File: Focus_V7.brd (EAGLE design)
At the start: 64.8 x 94 mm, 100 parts, among them X1 USB+SHIELD, Y1 16Mhz

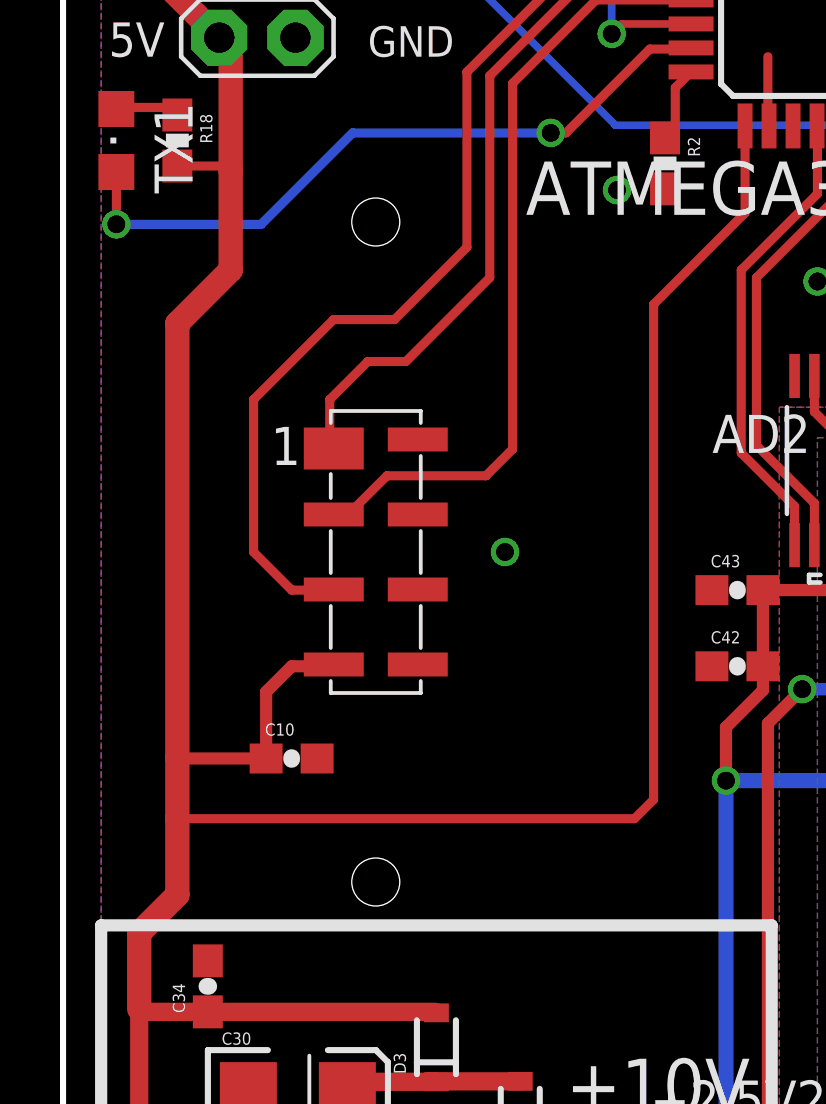
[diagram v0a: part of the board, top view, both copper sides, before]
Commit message: Changed hole size from 1.6 to 2.2mm for TSL1401CL shroud
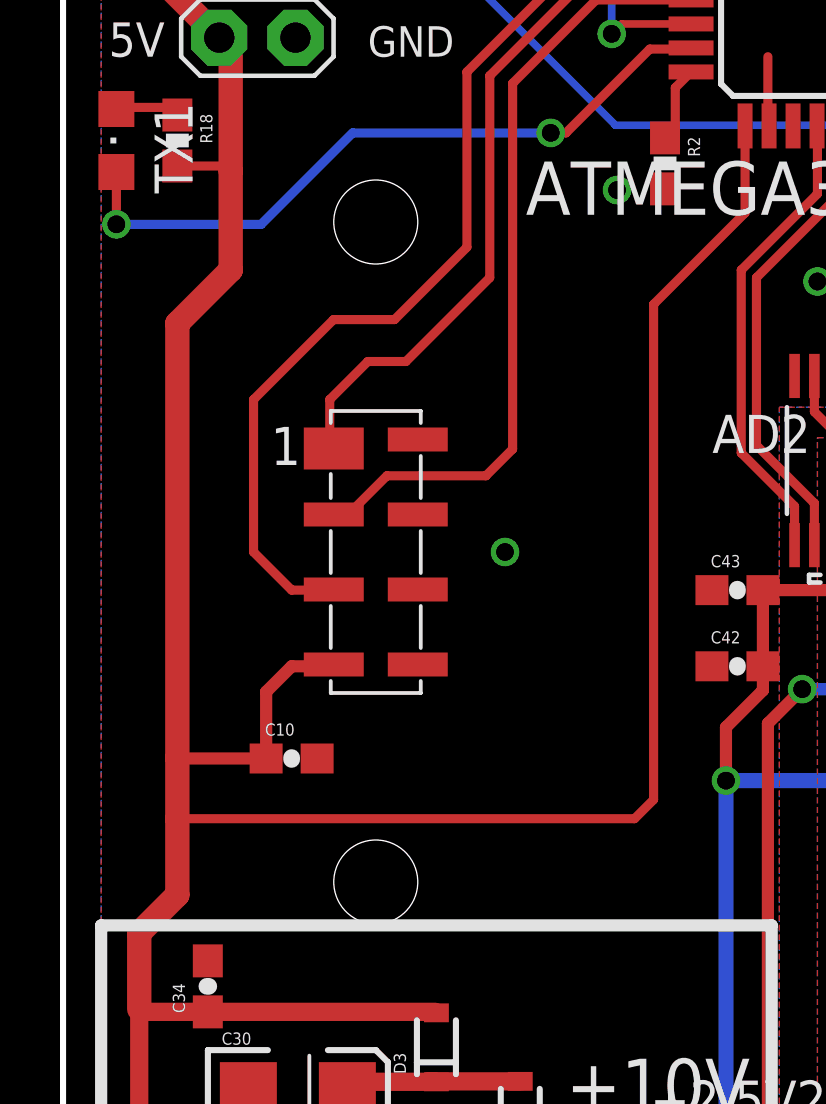
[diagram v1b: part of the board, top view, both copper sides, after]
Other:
- board text added: "Adafruit Industries"
- board text added: "Parallax Inc"
- board text added: "Sparkfun Electronics"
- board text removed: "Adafruit"
- board text removed: "Sparkfun"
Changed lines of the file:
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@@
 <layer number="50" name="dxf" color="7" fill="1" visible="no" active="yes"/>
 <layer number="51" name="tDocu" color="6" fill="1" visible="yes" active="yes"/>
-<layer number="52" name="bDocu" color="7" fill="1" visible="no" active="yes"/>
+<layer number="52" name="bDocu" color="7" fill="1" visible="yes" active="yes"/>
 <layer number="53" name="tGND_GNDA" color="7" fill="9" visible="no" active="no"/>
 <layer number="54" name="bGND_GNDA" color="1" fill="9" visible="no" active="no"/>
@@
 <hole x="96.52" y="2.54" drill="3.2"/>
 <text x="74.93" y="21.59" size="1.778" layer="22" rot="MR0">Arduino Team</text>
-<text x="74.93" y="17.78" size="1.778" layer="22" rot="MR0">Sparkfun</text>
-<text x="74.93" y="13.97" size="1.778" layer="22" rot="MR0">Adafruit</text>
+<text x="74.93" y="17.78" size="1.778" layer="22" rot="MR0">Sparkfun Electronics</text>
+<text x="74.93" y="13.97" size="1.778" layer="22" rot="MR0">Adafruit Industries</text>
 <wire x1="44.45" y1="24.13" x2="82.55" y2="24.13" width="0.254" layer="22"/>
 <wire x1="77.724" y1="32.512" x2="80.264" y2="32.512" width="0.3048" layer="41"/>
@@
 <wire x1="75.184" y1="66.167" x2="75.311" y2="66.294" width="0.3048" layer="42"/>
 <wire x1="76.581" y1="67.691" x2="76.708" y2="67.818" width="0.3048" layer="42"/>
+<text x="74.93" y="10.16" size="1.778" layer="22" rot="MR0">Parallax Inc</text>
 </plain>
 <attributes>
@@
 <via x="70.358" y="36.83" extent="1-16" drill="0.6"/>
 <via x="80.391" y="38.1" extent="1-16" drill="0.6"/>
+<wire x1="64.516" y1="51.5874" x2="63.1952" y2="51.5874" width="0" layer="19" extent="1-1"/>
 </signal>
 <signal name="TSL1401R_A0">

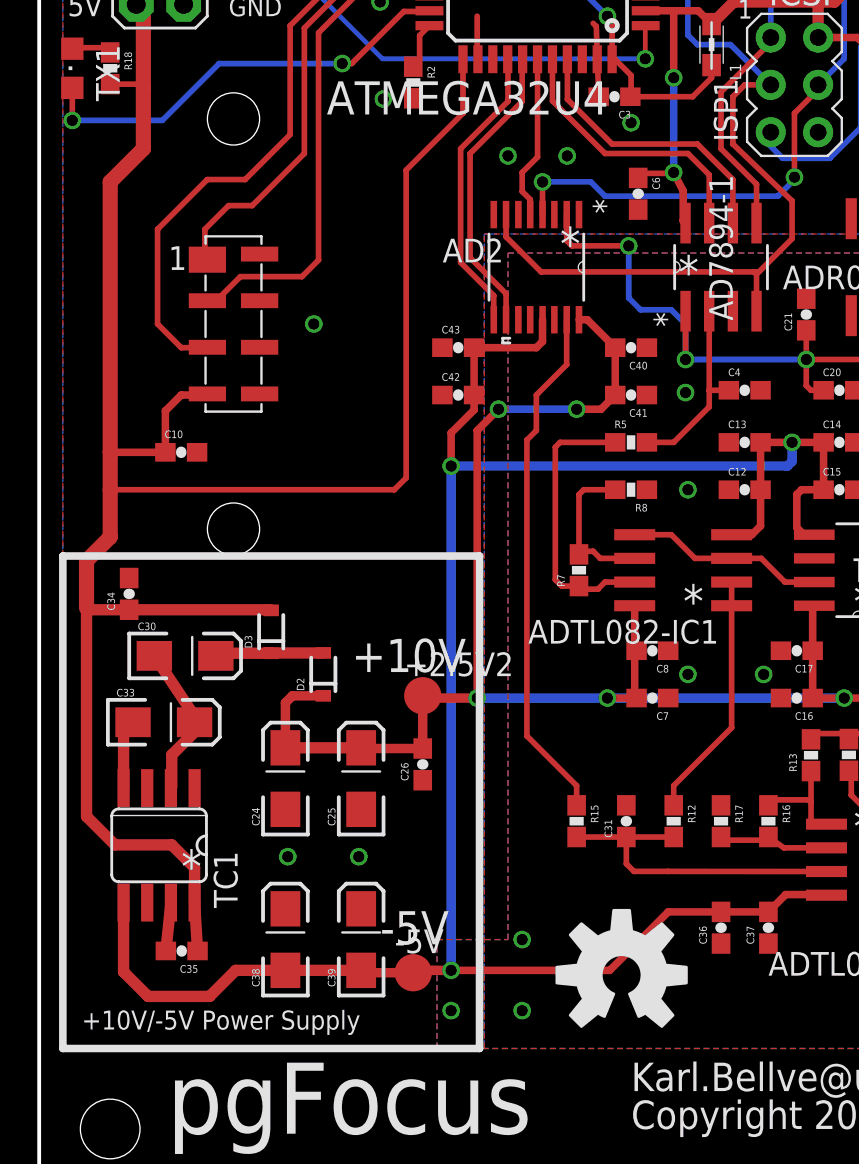
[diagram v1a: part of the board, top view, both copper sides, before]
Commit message: Pin 7 of TC7660 has a capacitor labeled C35, which should have been connected to ground, and not 5V This has been corrected in this revision. C35 is optional, and not needed. Only use if trying to slow down OSC for lower current.
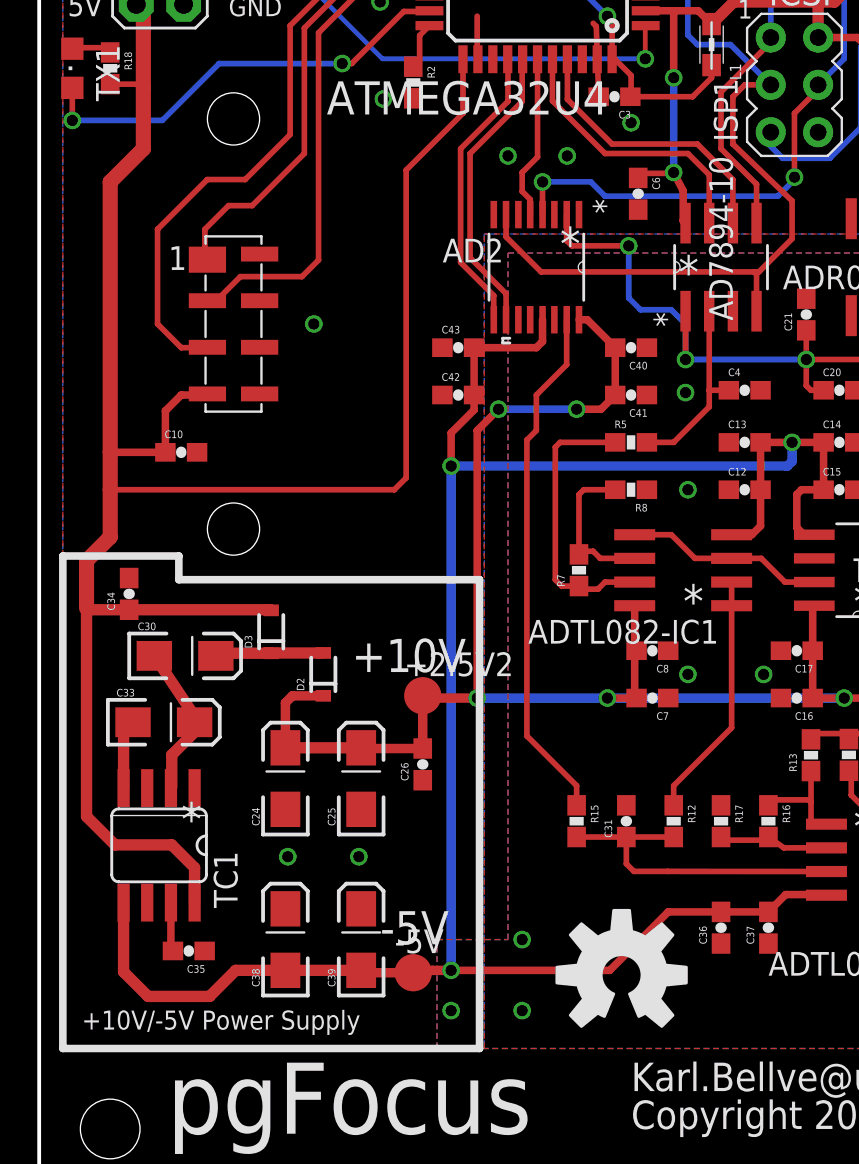
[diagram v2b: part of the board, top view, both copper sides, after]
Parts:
- moved C35 0.38 mm to (43.6, 12.1)
- renumbered AD7894-1 to AD7894-10
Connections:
- net +5V: no longer C35.1
- net GND: now also C35.1
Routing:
- net +5V: track 324.1 -> 321.5 mm
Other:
- board text added: "Optional Cap (C35) to"
- board text added: "slow the OSC (pin 7)"
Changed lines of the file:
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@@
 <layer number="39" name="tKeepout" color="4" fill="11" visible="no" active="yes"/>
 <layer number="40" name="bKeepout" color="1" fill="11" visible="no" active="yes"/>
-<layer number="41" name="tRestrict" color="4" fill="10" visible="no" active="yes"/>
-<layer number="42" name="bRestrict" color="1" fill="10" visible="no" active="yes"/>
+<layer number="41" name="tRestrict" color="4" fill="10" visible="yes" active="yes"/>
+<layer number="42" name="bRestrict" color="1" fill="10" visible="yes" active="yes"/>
 <layer number="43" name="vRestrict" color="2" fill="10" visible="no" active="yes"/>
 <layer number="44" name="Drills" color="7" fill="1" visible="no" active="yes"/>
@@
 <layer number="50" name="dxf" color="7" fill="1" visible="no" active="yes"/>
 <layer number="51" name="tDocu" color="6" fill="1" visible="yes" active="yes"/>
-<layer number="52" name="bDocu" color="7" fill="1" visible="yes" active="yes"/>
+<layer number="52" name="bDocu" color="7" fill="1" visible="no" active="yes"/>
 <layer number="53" name="tGND_GNDA" color="7" fill="9" visible="no" active="no"/>
 <layer number="54" name="bGND_GNDA" color="1" fill="9" visible="no" active="no"/>
@@
 <wire x1="94.488" y1="46.228" x2="95.123" y2="44.831" width="0.3048" layer="42"/>
 <wire x1="95.123" y1="44.831" x2="94.996" y2="43.18" width="0.3048" layer="42"/>
-<wire x1="59.182" y1="33.274" x2="36.83" y2="33.274" width="0.4064" layer="21"/>
-<wire x1="59.182" y1="33.274" x2="59.182" y2="6.858" width="0.4064" layer="21"/>
+<wire x1="59.182" y1="32.004" x2="43.053" y2="32.004" width="0.4064" layer="21"/>
+<wire x1="43.053" y1="32.004" x2="43.053" y2="33.274" width="0.4064" layer="21"/>
+<wire x1="43.053" y1="33.274" x2="36.83" y2="33.274" width="0.4064" layer="21"/>
+<wire x1="59.182" y1="32.004" x2="59.182" y2="6.858" width="0.4064" layer="21"/>
 <wire x1="76.708" y1="14.478" x2="80.01" y2="14.478" width="0.254" layer="41"/>
 <wire x1="68.326" y1="29.972" x2="72.136" y2="29.972" width="0.3048" layer="41"/>
@@
 <text x="85.852" y="39.116" size="1.778" layer="21" font="vector" ratio="15" rot="R90">+2.5V</text>
 <text x="77.216" y="73.152" size="1.778" layer="21" font="vector" ratio="15" rot="R180">+5V</text>
-<text x="43.18" y="15.748" size="1.778" layer="21" font="vector" ratio="15">*</text>
+<text x="43.18" y="18.288" size="1.778" layer="21" font="vector" ratio="15">*</text>
 <text x="67.31" y="2.54" size="1.524" layer="21" font="vector" ratio="15">Copyright 2013</text>
 <text x="63.5" y="49.149" size="1.778" layer="21" font="vector" ratio="15">*</text>
@@
 <hole x="39.37" y="2.54" drill="3.2"/>
 <hole x="96.52" y="2.54" drill="3.2"/>
-<text x="74.93" y="21.59" size="1.778" layer="22" rot="MR0">Arduino Team</text>
-<text x="74.93" y="17.78" size="1.778" layer="22" rot="MR0">Sparkfun Electronics</text>
-<text x="74.93" y="13.97" size="1.778" layer="22" rot="MR0">Adafruit Industries</text>
+<text x="74.93" y="21.59" size="1.778" layer="22" ratio="15" rot="MR0">Arduino Team</text>
+<text x="74.93" y="17.78" size="1.778" layer="22" ratio="15" rot="MR0">Sparkfun Electronics</text>
+<text x="74.93" y="13.97" size="1.778" layer="22" ratio="15" rot="MR0">Adafruit Industries</text>
 <wire x1="44.45" y1="24.13" x2="82.55" y2="24.13" width="0.254" layer="22"/>
 <wire x1="77.724" y1="32.512" x2="80.264" y2="32.512" width="0.3048" layer="41"/>
@@
 <wire x1="75.184" y1="66.167" x2="75.311" y2="66.294" width="0.3048" layer="42"/>
 <wire x1="76.581" y1="67.691" x2="76.708" y2="67.818" width="0.3048" layer="42"/>
-<text x="74.93" y="10.16" size="1.778" layer="22" rot="MR0">Parallax Inc</text>
+<text x="74.93" y="10.16" size="1.778" layer="22" ratio="15" rot="MR0">Parallax Inc</text>
+<text x="33.02" y="10.16" size="1.016" layer="51" rot="R90">Optional Cap (C35) to</text>
+<text x="34.29" y="10.16" size="1.016" layer="51" rot="R90">slow the OSC (pin 7)</text>
 </plain>
 <attributes>
@@
 <attribute name="VALUE" x="77.089" y="50.673" size="1.27" layer="27" rot="R270"/>
 </element>
-<element name="AD7894-1" library="BIG" package="R_8" value="AD7894ARZ-3" x="72.136" y="48.768" rot="R90">
+<element name="AD7894-10" library="BIG" package="R_8" value="AD7894ARZ-3" x="72.136" y="48.768" rot="R90">
 <attribute name="MANUFACTURER_PART_NUMBER" value="AD7894ARZ-3" x="72.136" y="48.768" size="1.778" layer="27" rot="R90" display="off"/>
 <attribute name="VENDOR" value="Vendor" x="72.136" y="48.768" size="1.778" layer="27" rot="R90" display="off"/>
@@
 <element name="L2" library="wuerth-elektronik" package="0805" value="WE-CBF 0805" x="81.534" y="76.962" rot="R270"/>
 <element name="F1" library="SparkFun" package="PTC-1206" value="PTCSMD" x="83.766" y="80.523" rot="R180"/>
-<element name="C35" library="SparkFun" package="0603-CAP" value="0.1uF" x="43.206" y="12.089" rot="R180"/>
+<element name="C35" library="SparkFun" package="0603-CAP" value="0.1uF" x="43.587" y="12.089" rot="R180"/>
 <element name="C4" library="SparkFun" package="0603-CAP" value="0.1uF" x="73.406" y="42.164"/>
 <element name="R5" library="SparkFun" package="0603-RES" value="300" x="67.31" y="39.37"/>
@@
 <contactref element="C14" pad="2"/>
 <contactref element="C16" pad="2"/>
-<contactref element="AD7894-1" pad="3"/>
+<contactref element="AD7894-10" pad="3"/>
 <contactref element="AD2" pad="8"/>
 <contactref element="C21" pad="2"/>
@@
 <via x="70.358" y="36.83" extent="1-16" drill="0.6"/>
 <via x="80.391" y="38.1" extent="1-16" drill="0.6"/>
+<contactref element="C35" pad="1"/>
 <wire x1="64.516" y1="51.5874" x2="63.1952" y2="51.5874" width="0" layer="19" extent="1-1"/>
 </signal>
@@
 <contactref element="ATMEGA32U4" pad="9"/>
 <contactref element="ISP1" pad="3"/>
-<contactref element="AD7894-1" pad="4"/>
+<contactref element="AD7894-10" pad="4"/>
 <wire x1="74.803" y1="58.547" x2="72.644" y2="60.706" width="0.3048" layer="16"/>
 <wire x1="72.644" y1="60.706" x2="70.866" y2="60.706" width="0.3048" layer="16"/>
@@
 <contactref element="ATMEGA32U4" pad="11"/>
 <contactref element="ISP1" pad="1"/>
-<contactref element="AD7894-1" pad="5"/>
+<contactref element="AD7894-10" pad="5"/>
 <wire x1="74.803" y1="61.087" x2="74.803" y2="65.786" width="0.3048" layer="16"/>
 <wire x1="68.834" y1="71.755" x2="68.834" y2="70.462" width="0.3048" layer="1"/>
@@
 </signal>
 <signal name="+5V">
-<contactref element="TC1" pad="8"/>
-<contactref element="D3" pad="2"/>
 <contactref element="U$1" pad="VDD"/>
-<contactref element="AD7894-1" pad="8"/>
+<contactref element="AD7894-10" pad="8"/>
 <contactref element="C6" pad="1"/>
 <contactref element="C2" pad="1"/>
@@
 <contactref element="C10" pad="1"/>
 <contactref element="F1" pad="2"/>
-<contactref element="C35" pad="1"/>
-<contactref element="C34" pad="1"/>
 <contactref element="ISP1" pad="2"/>
 <contactref element="ATMEGA32U4" pad="34"/>
@@
 <contactref element="R1" pad="1"/>
 <contactref element="D1" pad="C"/>
-<wire x1="44.056" y1="12.089" x2="43.897" y2="14.6806" width="0.6096" layer="1"/>
 <wire x1="68.094" y1="62.522" x2="69.596" y2="62.522" width="0.4064" layer="1"/>
 <wire x1="72.814" y1="62.992" x2="77.47" y2="62.992" width="0.6096" layer="1"/>
@@
 <wire x1="39.624" y1="17.78" x2="38.1" y2="19.304" width="0.6096" layer="1"/>
 <wire x1="42.672" y1="17.78" x2="39.624" y2="17.78" width="0.6096" layer="1"/>
-<wire x1="43.897" y1="14.6806" x2="43.897" y2="16.555" width="0.6096" layer="1"/>
 <wire x1="43.897" y1="16.555" x2="42.672" y2="17.78" width="0.6096" layer="1"/>
-<wire x1="38.188" y1="30.392" x2="40.386" y2="30.392" width="0.6096" layer="1"/>
 <wire x1="38.1" y1="30.48" x2="38.188" y2="30.392" width="0.508" layer="1"/>
-<wire x1="40.386" y1="30.392" x2="47.974" y2="30.392" width="0.6096" layer="1"/>
-<wire x1="47.974" y1="30.392" x2="48.006" y2="30.36" width="0.508" layer="1"/>
 <wire x1="39.37" y1="34.29" x2="39.37" y2="36.83" width="0.8128" layer="1"/>
 <wire x1="39.37" y1="36.83" x2="39.37" y2="38.862" width="0.8128" layer="1"/>
@@
 <wire x1="70.104" y1="52.864" x2="69.596" y2="53.848" width="0.4064" layer="1"/>
 <wire x1="69.421" y1="53.8" x2="69.596" y2="53.848" width="0.4064" layer="1"/>
+<contactref element="TC1" pad="8"/>
+<contactref element="D3" pad="2"/>
+<contactref element="C34" pad="1"/>
+<wire x1="43.897" y1="16.555" x2="43.897" y2="14.6806" width="0.6096" layer="1"/>
+<wire x1="38.188" y1="30.392" x2="40.386" y2="30.392" width="0.6096" layer="1"/>
+<wire x1="40.386" y1="30.392" x2="47.974" y2="30.392" width="0.6096" layer="1"/>
+<wire x1="47.974" y1="30.392" x2="48.006" y2="30.36" width="0.6096" layer="1"/>
 </signal>
 <signal name="N$30">
@@
 <contactref element="C20" pad="1"/>
 <contactref element="ADR03BRZ" pad="6"/>
-<contactref element="AD7894-1" pad="1"/>
+<contactref element="AD7894-10" pad="1"/>
 <contactref element="C21" pad="1"/>
 <contactref element="+2.5V" pad="TP"/>
@@
 </signal>
 <signal name="ADC_BUSY">
-<contactref element="AD7894-1" pad="6"/>
+<contactref element="AD7894-10" pad="6"/>
 <contactref element="ATMEGA32U4" pad="41"/>
 <wire x1="63.894" y1="57.772" x2="63.894" y2="59.922" width="0.3048" layer="1"/>
@@
 <contactref element="TC1" pad="7"/>
 <contactref element="C35" pad="2"/>
-<wire x1="42.356" y1="12.089" x2="42.627" y2="14.6806" width="0.6096" layer="1"/>
+<wire x1="42.627" y1="14.6806" x2="42.627" y2="12.199" width="0.4064" layer="1"/>
+<wire x1="42.627" y1="12.199" x2="42.737" y2="12.089" width="0.4064" layer="1"/>
 </signal>
 <signal name="ADC_CONVST">
-<contactref element="AD7894-1" pad="7"/>
+<contactref element="AD7894-10" pad="7"/>
 <contactref element="ATMEGA32U4" pad="40"/>
 <wire x1="63.0936" y1="57.6834" x2="63.094" y2="59.922" width="0.3048" layer="1"/>
@@
 </signal>
 <signal name="N$3">
-<contactref element="AD7894-1" pad="2"/>
+<contactref element="AD7894-10" pad="2"/>
 <contactref element="C4" pad="1"/>
 <contactref element="R5" pad="2"/>
